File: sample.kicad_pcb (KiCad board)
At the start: 2 copper layers, 35 parts, among them CN10 Conn_02x17_Odd_Even, CN7 Conn_02x10_Odd_Even, CN8 Conn_02x08_Odd_Even, CN9 Conn_02x15_Odd_Even, U1 TJA1042T-3, U2 TJA1042T-3, U3 TJA1042T-3

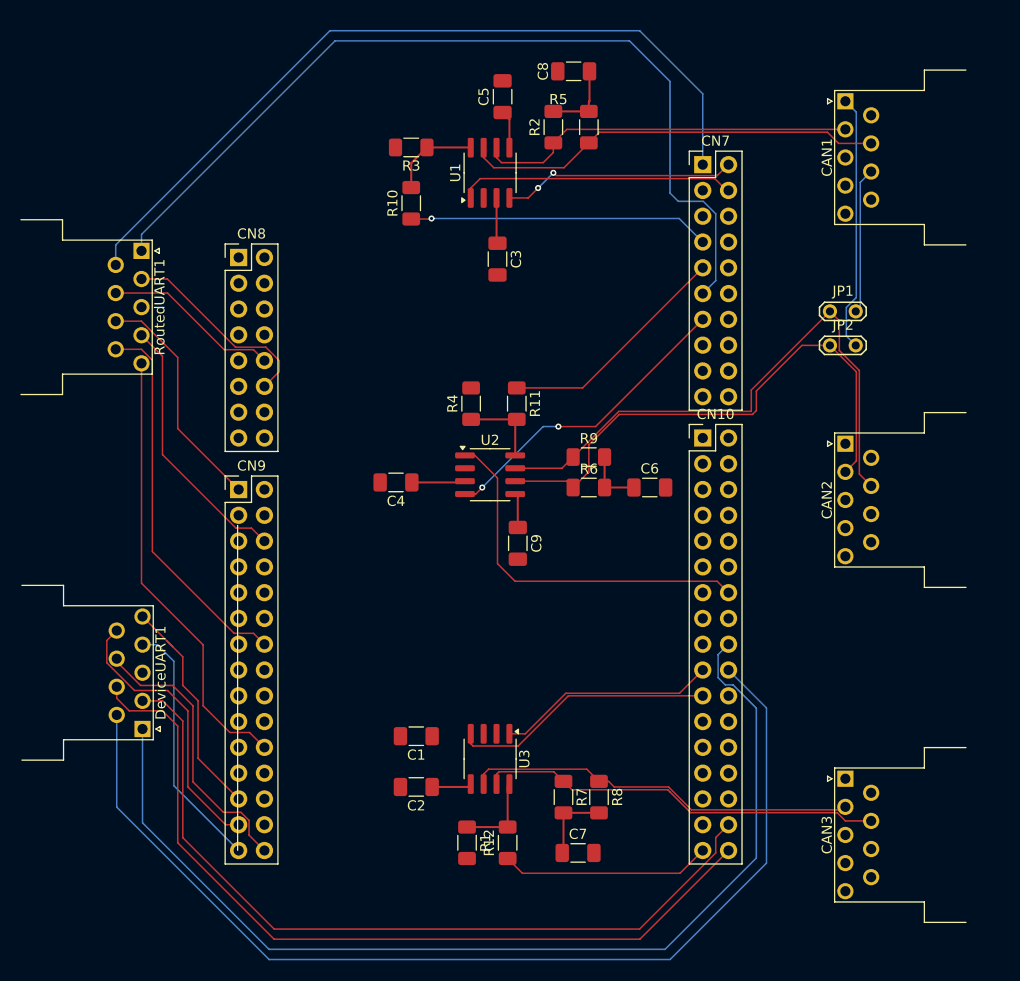
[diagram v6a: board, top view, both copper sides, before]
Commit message: All nets conected except GND
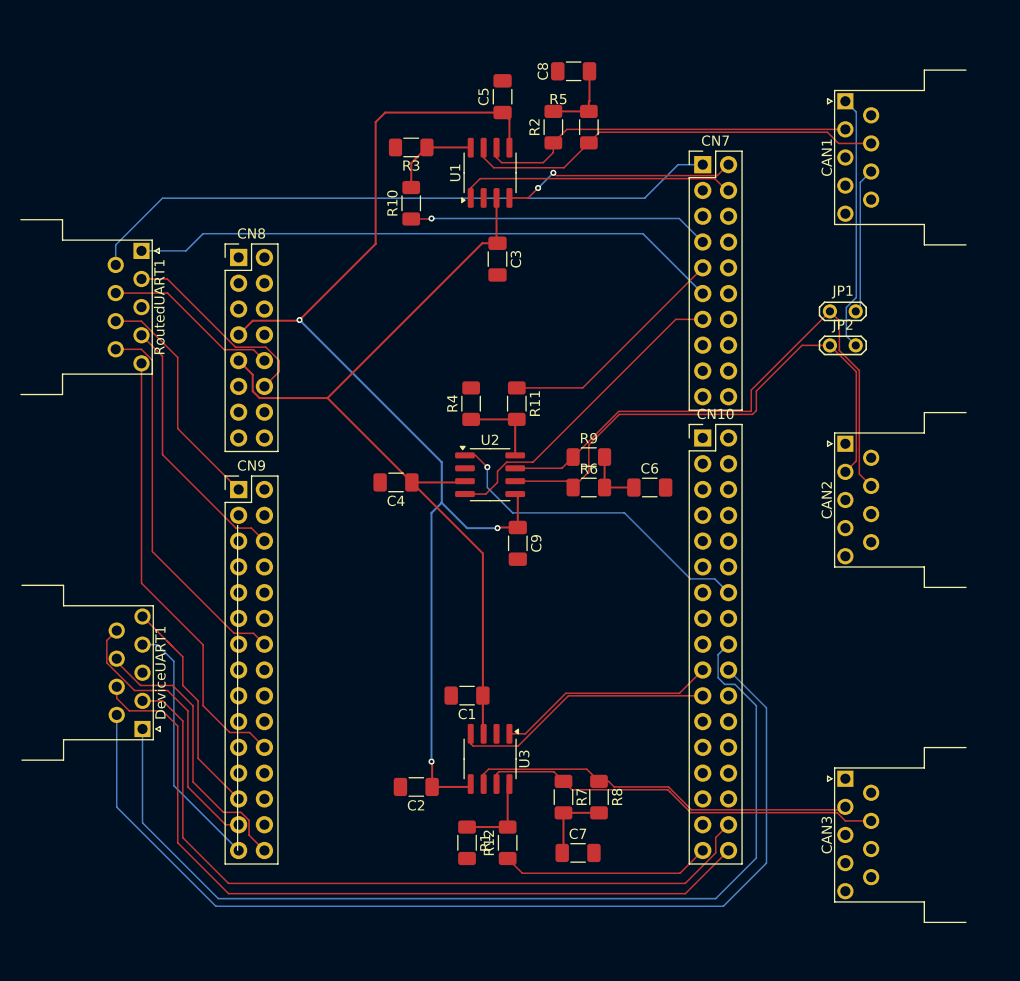
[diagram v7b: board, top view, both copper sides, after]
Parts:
- moved C1 6.40 mm to (126.0, 111.5)
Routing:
- net +3V3: track 11.1 -> 114.0 mm, vias 0 -> 3
- net +5V: track 9.79 -> 83.5 mm
- net USART6_RX: track 88.0 -> 58.4 mm
- net USART6_TX: track 78.1 -> 63.1 mm
- net UART7_RX: track 103.8 -> 99.5 mm
- net UART7_TX: track 102.1 -> 98.1 mm
- net CAN2_TX: track 36.5 -> 32.7 mm, vias 0 -> 1
- net USART3_TX: track 78.9 -> 75.2 mm
- net USART3_RX: track 81.6 -> 77.9 mm
- net CAN2_RX: track 30.6 -> 31.2 mm, vias 2 -> 0

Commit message: add copper fill
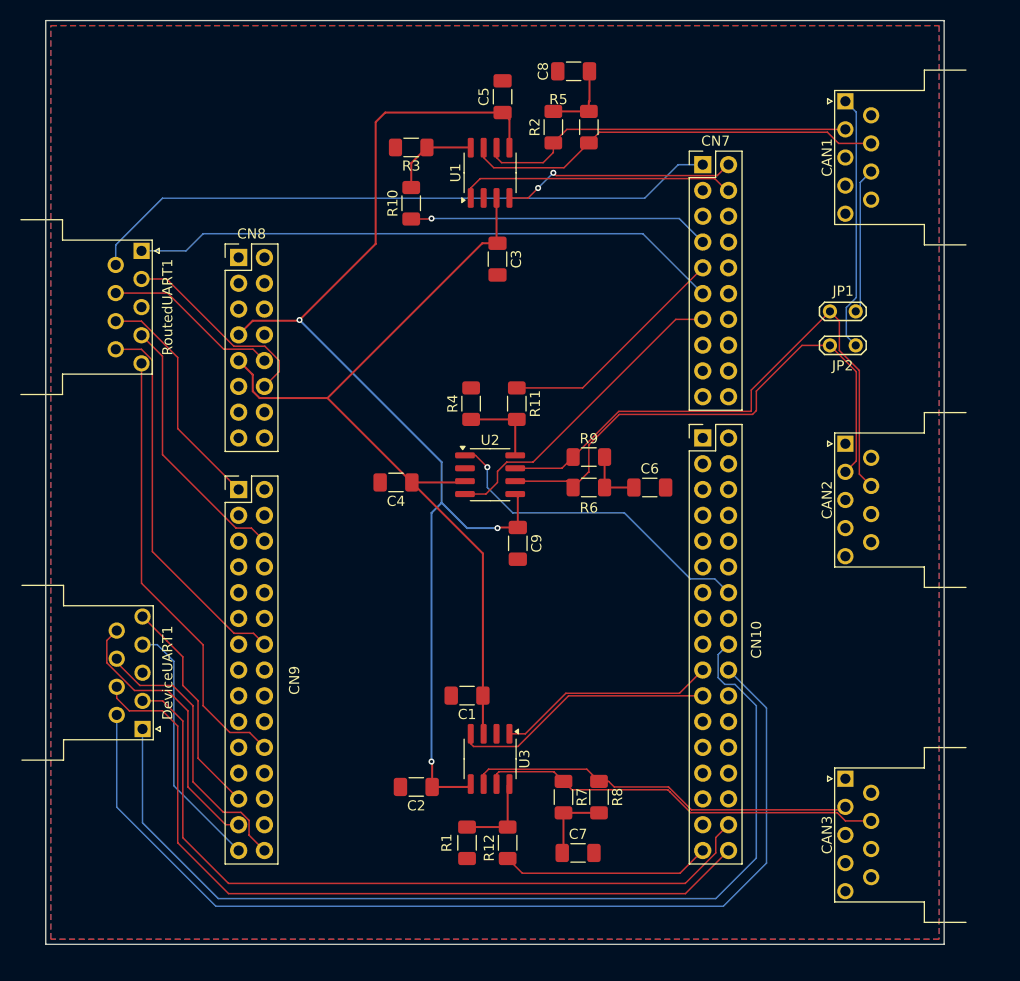
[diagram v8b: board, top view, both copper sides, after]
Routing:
- net UART4_RX: track 22.7 -> 21.9 mm
- added copper zone on B.Cu, net GND
- added copper zone on F.Cu, net GND
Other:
- board outline added: 88.5 x 91 mm
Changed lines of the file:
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@@
 		(tags "resistor handsolder")
 		(property "Reference" "R1"
-			(at 0 -1.82 90)
+			(at 0 2 90)
 			(layer "F.SilkS")
 			(effects
@@
 		(tags "Through hole pin header THT 2x15 2.54mm double row")
 		(property "Reference" "CN9"
-			(at 1.27 -2.33 0)
+			(at 5.5 18.8 90)
 			(layer "F.SilkS")
 			(effects
@@
 		(tags "CONN DEV")
 		(property "Reference" "JP2"
-			(at 1.3 -2 0)
+			(at 1.25 2 0)
 			(layer "F.SilkS")
 			(effects
@@
 		(tags "resistor handsolder")
 		(property "Reference" "R6"
-			(at 0 -1.82 360)
+			(at 0 2 360)
 			(layer "F.SilkS")
 			(effects
@@
 		(tags "9-pin D-Sub connector horizontal angled 90deg THT male pitch 2.77x2.54mm pin-PCB-offset 9.4mm")
 		(property "Reference" "RoutedUART1"
-			(at 5.54 -1.8 90)
+			(at 5.54 -2.569669 90)
 			(layer "F.SilkS")
 			(effects
@@
 		(tags "Through hole pin header THT 2x17 2.54mm double row")
 		(property "Reference" "CN10"
-			(at 1.27 -2.33 0)
+			(at 5.28 19.88 90)
 			(layer "F.SilkS")
 			(effects
@@
 		(tags "9-pin D-Sub connector horizontal angled 90deg THT female pitch 2.77x2.54mm pin-PCB-offset 9.4mm")
 		(property "Reference" "DeviceUART1"
-			(at -5.54 -1.8 90)
+			(at -5.54 -2.469669 90)
 			(layer "F.SilkS")
 			(effects
@@
 		(tags "resistor handsolder")
 		(property "Reference" "R12"
-			(at 0 -1.82 270)
+			(at -0.5 -1.82 270)
 			(layer "F.SilkS")
 			(effects
@@
 		)
 	)
-	(gr_line
-		(start 103.4 126.74)
-		(end 103.4 94.74)
+	(gr_rect
+		(start 84.5 45)
+		(end 173 136)
 		(stroke
-			(width 0.1)
+			(width 0.05)
 			(type default)
 		)
-		(layer "F.SilkS")
+		(fill none)
+		(layer "Edge.Cuts")
 	)
 	(segment
@@
 	)
 	(segment
-		(start 126.365 115.265)
-		(end 126.365 116.239999)
+		(start 136 111.52)
+		(end 149.22 111.52)
 		(width 0.15)
 		(layer "F.Cu")
@@
 	)
 	(segment
-		(start 126.590001 116.465)
-		(end 131.035 116.465)
+		(start 126.640001 116.515)
+		(end 131.005 116.515)
 		(width 0.15)
 		(layer "F.Cu")
@@
 	)
 	(segment
-		(start 135.98 111.52)
-		(end 149.22 111.52)
+		(start 131.005 116.515)
+		(end 136 111.52)
 		(width 0.15)
 		(layer "F.Cu")
@@
 	)
 	(segment
-		(start 131.035 116.465)
-		(end 135.98 111.52)
+		(start 126.365 115.265)
+		(end 126.365 116.239999)
 		(width 0.15)
 		(layer "F.Cu")
@@
 	(segment
 		(start 126.365 116.239999)
-		(end 126.590001 116.465)
+		(end 126.640001 116.515)
 		(width 0.15)
 		(layer "F.Cu")
@@
 	)
 	(segment
-		(start 104.965 77.425)
-		(end 102.08 77.425)
+		(start 96.5 71.845)
+		(end 91.390331 71.845)
 		(width 0.15)
 		(layer "F.Cu")
@@
 	(segment
 		(start 106.04 78.5)
-		(end 104.965 77.425)
+		(end 104.915 77.375)
 		(width 0.15)
 		(layer "F.Cu")
@@
 	)
 	(segment
-		(start 91.390331 71.845)
-		(end 96.5 71.845)
+		(start 104.915 77.375)
+		(end 102.03 77.375)
 		(width 0.15)
 		(layer "F.Cu")
@@
 	)
 	(segment
-		(start 102.08 77.425)
+		(start 102.03 77.375)
 		(end 96.5 71.845)
 		(width 0.15)
@@
 	)
 	(segment
-		(start 97 106.679669)
-		(end 96.410165 106.089835)
-		(width 0.15)
-		(layer "F.Cu")
-		(net 98)
-	)
-	(segment
 		(start 98 107.67967)
 		(end 98 110.5)
@@
 	)
 	(segment
-		(start 93.930331 70.46)
-		(end 96.47972 70.46)
+		(start 103.034009 77.085)
+		(end 106.085 77.085)
 		(width 0.15)
 		(layer "F.Cu")
@@
 	)
 	(segment
-		(start 107.5 78.5)
-		(end 107.5 79.58)
+		(start 107.5 79.58)
+		(end 106.04 81.04)
 		(width 0.15)
 		(layer "F.Cu")
@@
 	)
 	(segment
-		(start 103.19472 77.175)
-		(end 106.175 77.175)
+		(start 107.5 78.5)
+		(end 107.5 79.58)
 		(width 0.15)
 		(layer "F.Cu")
@@
 	)
 	(segment
-		(start 107.5 79.58)
-		(end 106.04 81.04)
+		(start 106.085 77.085)
+		(end 107.5 78.5)
 		(width 0.15)
 		(layer "F.Cu")
@@
 	)
 	(segment
-		(start 106.175 77.175)
-		(end 107.5 78.5)
+		(start 93.930331 70.46)
+		(end 96.409009 70.46)
 		(width 0.15)
 		(layer "F.Cu")
@@
 	)
 	(segment
-		(start 96.47972 70.46)
-		(end 103.19472 77.175)
+		(start 96.409009 70.46)
+		(end 103.034009 77.085)
 		(width 0.15)
 		(layer "F.Cu")
@@
 	)
 	(segment
-		(start 93.830762 110.5)
+		(start 99 112.5)
 		(end 97 110.5)
 		(width 0.15)
@@
 	)
 	(segment
-		(start 91.490331 107.865)
-		(end 91.490331 108.159569)
+		(start 104.525 125.245)
+		(end 104.525 123.795431)
 		(width 0.15)
 		(layer "F.Cu")
@@
 	)
 	(segment
-		(start 104.525 123.795431)
-		(end 104.525 125.245)
+		(start 97 110.5)
+		(end 93.760051 110.5)
 		(width 0.15)
 		(layer "F.Cu")
@@
 	)
 	(segment
-		(start 103.729569 123)
-		(end 104.525 123.795431)
+		(start 93.760051 110.5)
+		(end 91.490331 108.23028)
 		(width 0.15)
 		(layer "F.Cu")
@@
 	)
 	(segment
-		(start 97 110.5)
-		(end 99 112.5)
+		(start 91.490331 108.23028)
+		(end 91.490331 107.865)
 		(width 0.15)
 		(layer "F.Cu")
@@
 	)
 	(segment
-		(start 91.490331 108.159569)
-		(end 93.830762 110.5)
+		(start 106.04 126.76)
+		(end 104.525 125.245)
 		(width 0.15)
 		(layer "F.Cu")
@@
 	)
 	(segment
-		(start 102 123)
-		(end 103.729569 123)
+		(start 99 120)
+		(end 99 112.5)
 		(width 0.15)
 		(layer "F.Cu")
@@
 	)
 	(segment
-		(start 104.525 125.245)
-		(end 106.04 126.76)
+		(start 102 123)
+		(end 99 120)
 		(width 0.15)
 		(layer "F.Cu")
@@
 	)
 	(segment
-		(start 99 112.5)
-		(end 99 120)
+		(start 103.729569 123)
+		(end 102 123)
 		(width 0.15)
 		(layer "F.Cu")
@@
 	)
 	(segment
-		(start 99 120)
-		(end 102 123)
+		(start 104.525 123.795431)
+		(end 103.729569 123)
 		(width 0.15)
 		(layer "F.Cu")
@@
 		(net 116)
 	)
+	(zone
+		(net 3)
+		(net_name "GND")
+		(layers "F&B.Cu")
+		(hatch edge 0.5)
+		(connect_pads
+			(clearance 0.15)
+		)
+		(min_thickness 0.15)
+		(filled_areas_thickness no)
+		(fill yes
+			(thermal_gap 0.3)
+			(thermal_bridge_width 0.3)
+		)
+		(polygon
+			(pts
+				(xy 172.5 45.5) (xy 172.5 135.5) (xy 85 135.5) (xy 85 45.5)
+			)
+		)
+	)
 )
